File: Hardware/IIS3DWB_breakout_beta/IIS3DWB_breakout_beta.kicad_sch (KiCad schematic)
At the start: 7 parts, among them J1 5051100892, U1 IIS3DWB

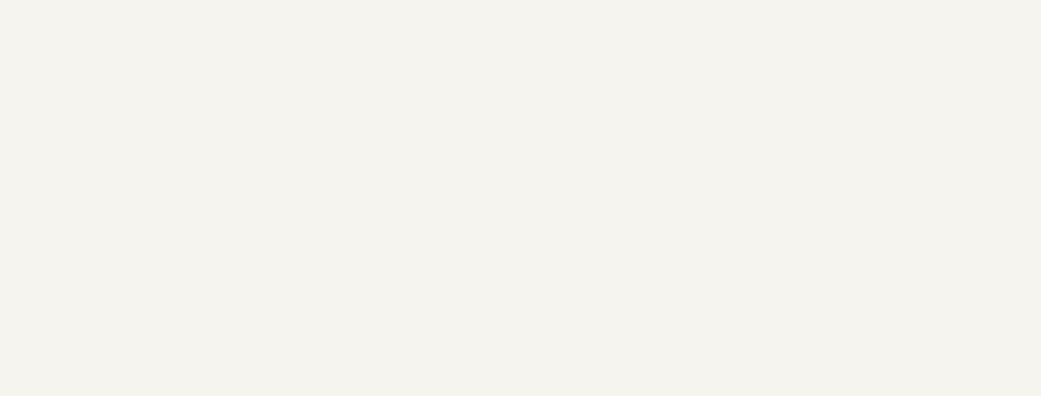
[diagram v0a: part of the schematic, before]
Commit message: Add hardware license and fix BOM issues
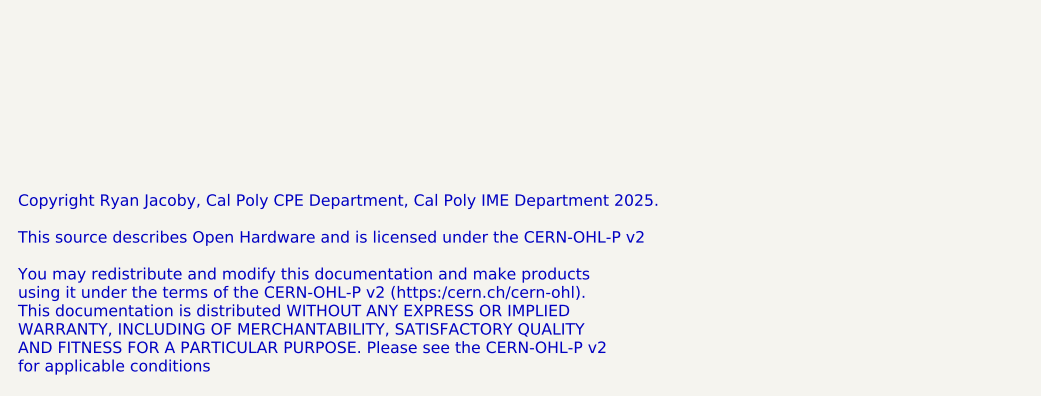
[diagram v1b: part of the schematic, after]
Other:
- note added: "Copyright Ryan Jacoby, Cal Poly CPE Department, Cal Poly IME Department 2025. This source describes Open Hardware and is licensed under the CERN-OHL-P v2 You may redistribute and modify this documentation and make products using it under the terms of the CERN-OHL-P v2 (https:/cern.ch/cern-ohl). This documentation is distributed WITHOUT ANY EXPRESS OR IMPLIED WARRANTY, INCLUDING OF MERCHANTABILITY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"
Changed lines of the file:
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@@
 		(comment 1 "Ryan Jacoby")
+	)
+	(text "Copyright Ryan Jacoby, Cal Poly CPE Department, Cal Poly IME Department 2025.\n\nThis source describes Open Hardware and is licensed under the CERN-OHL-P v2\n\nYou may redistribute and modify this documentation and make products\nusing it under the terms of the CERN-OHL-P v2 (https:/cern.ch/cern-ohl).\nThis documentation is distributed WITHOUT ANY EXPRESS OR IMPLIED\nWARRANTY, INCLUDING OF MERCHANTABILITY, SATISFACTORY QUALITY\nAND FITNESS FOR A PARTICULAR PURPOSE. Please see the CERN-OHL-P v2\nfor applicable conditions"
+		(exclude_from_sim no)
+		(at 18.542 184.15 0)
+		(effects
+			(font
+				(size 1.27 1.27)
+			)
+			(justify left)
+		)
 	)
 	(text "Pull-up disables SPI and enables I2C;\nto disable I2C, SPI CS can be pulled low"
